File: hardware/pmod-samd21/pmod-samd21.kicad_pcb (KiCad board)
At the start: 2 copper layers, 18 x 29 mm, 19 parts, among them J1 PMOD-2x6-MALE, J2 PMOD-2x6-FEMALE, J3 USB_C_Receptacle_USB2.0, Q1 2N7002PW, U1 ATSAMD21G-A, Y1 32.768kHz

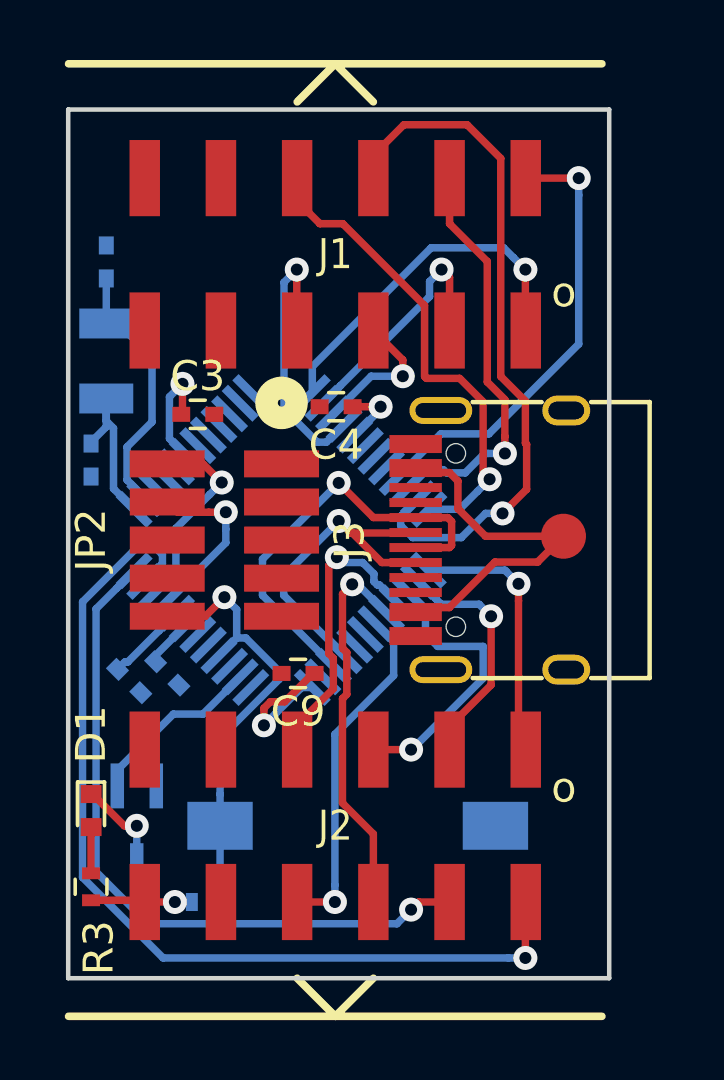
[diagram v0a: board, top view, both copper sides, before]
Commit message: PCB fully routed with DRC errors ignored - oshpark doesn't like the slots in the usb connector - need to check FET pinout
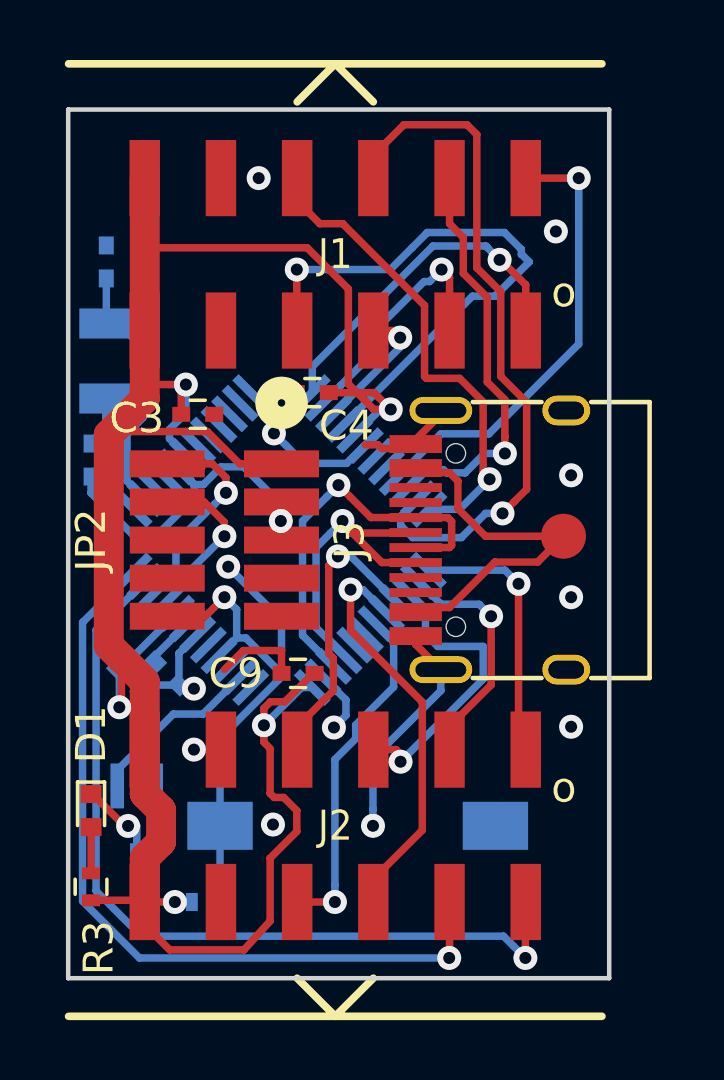
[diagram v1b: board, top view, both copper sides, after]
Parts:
- moved C4 0.92 mm to (150.9, 144.3)
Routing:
- net +3V3: track 17.1 -> 80.4 mm, vias 4 -> 5
- net GND: track 0.30 -> 39.0 mm, vias 0 -> 13
- net /SER0_3: track 9.57 -> 19.2 mm
- net /SER5_0: track 31.7 -> 28.1 mm
- net /SER5_1: track 23.4 -> 26.6 mm
- net /USB_D+: track 14.5 -> 13.3 mm
- net /USB_D-: track 11.9 -> 11.0 mm
- net /SER5_2: track 12.8 -> 13.6 mm
- net /SER1_2: track 9.45 -> 9.95 mm
- added copper zone on B.Cu, net GND
- added copper zone on F.Cu, net GND

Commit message: pcb as submitted to oshpark
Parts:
- TP1: moved to B.Cu
- moved J3 0.40 mm to (157.9, 149.2)
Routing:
- net /SER0_3: track 19.2 -> 9.57 mm
- net GND: track 39.0 -> 46.7 mm, vias 13 -> 12
- net /SER2_2: track 23.5 -> 27.6 mm
- net /SER1_2: track 9.95 -> 6.22 mm
- net /SER2_0: track 15.2 -> 12.8 mm
- net VBUS: track 12.9 -> 11.2 mm, vias 0 -> 1
- net /SER1_1: track 7.92 -> 9.58 mm
- net /SER5_2: track 13.6 -> 12.1 mm
- net /SER2_3: track 16.2 -> 17.6 mm
- net /SER2_1: track 13.7 -> 15.0 mm
- net /USB_D-: track 11.0 -> 11.9 mm
- net /SER5_3: track 11.6 -> 12.2 mm
- net /SER1_3: track 9.74 -> 9.17 mm
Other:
- board size 18 x 29 mm -> 18.2 x 29 mm
- board text added: "Nov 2018"
- board text added: "pmod-samd21"
- board text added: "tom@tomk.in"

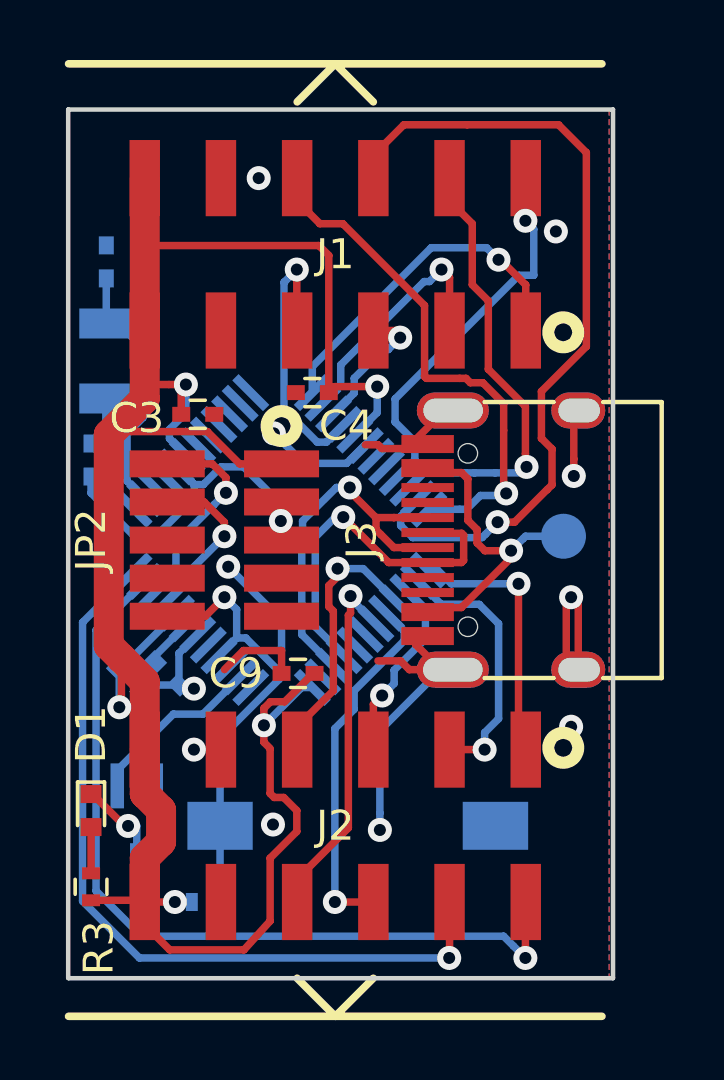
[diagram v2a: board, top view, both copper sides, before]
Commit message: pmod-samd21 : Fixed edge cuts for panelisation with plated slots
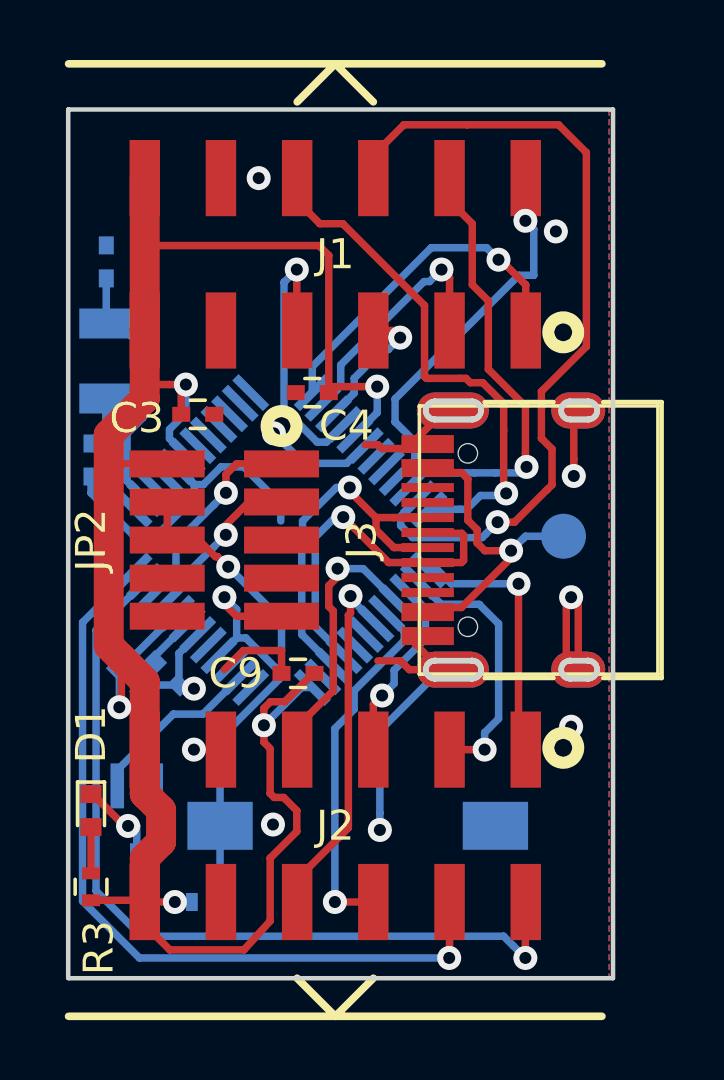
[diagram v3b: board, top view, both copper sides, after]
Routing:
- net GND: track 46.7 -> 50.4 mm, vias 12 -> 11
- net +3V3: track 80.8 -> 77.5 mm
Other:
- board text added: "Dec 2018"
- board text removed: "Nov 2018"

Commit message: pmod-samd21 - added missing usb C resistors - generated gerbers relative to aux origin
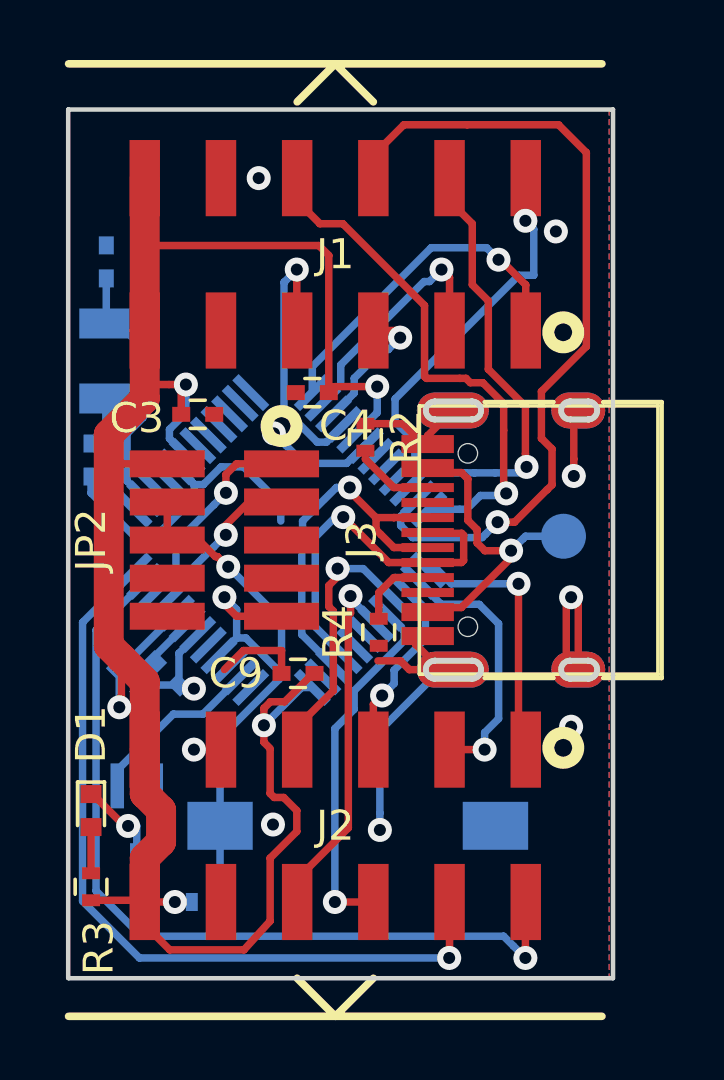
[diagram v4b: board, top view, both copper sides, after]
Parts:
- added R2: 5.1k, Resistors_SMD:R_0402, F.Cu at (152.7, 145.8)
- added R4: 5.1k, Resistors_SMD:R_0402, F.Cu at (153.1, 152.3)
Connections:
- J3 pad A5: (no net) -> Net-(J3-PadA5)
- J3 pad B5: (no net) -> Net-(J3-PadB5)
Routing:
- net Net-(J3-PadA5): track 0.00 -> 2.71 mm
- net Net-(J3-PadB5): track 0.00 -> 2.49 mm
- net GND: track 50.4 -> 51.2 mm
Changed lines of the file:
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@@
     (thickness 1.6)
     (drawings 8)
-    (tracks 413)
+    (tracks 420)
     (zones 0)
-    (modules 19)
-    (nets 31)
+    (modules 21)
+    (nets 33)
   )
   (page A4)
@@
     (pad_to_mask_clearance 0.051)
     (solder_mask_min_width 0.25)
-    (aux_axis_origin 0 0)
+    (aux_axis_origin 142.748 163.8173)
     (visible_elements FFFFFF7F)
     (pcbplotparams
@@
       (viasonmask false)
       (mode 1)
-      (useauxorigin false)
+      (useauxorigin true)
       (hpglpennumber 1)
       (hpglpenspeed 20)
@@
   (net 29 "Net-(D1-Pad1)")
   (net 30 "Net-(D1-Pad2)")
+  (net 31 "Net-(J3-PadB5)")
+  (net 32 "Net-(J3-PadA5)")
   (net_class Default "This is the default net class."
     (clearance 0.2)
@@
     (add_net "Net-(D1-Pad1)")
     (add_net "Net-(D1-Pad2)")
+    (add_net "Net-(J3-PadA5)")
+    (add_net "Net-(J3-PadB5)")
     (add_net VBUS)
   )
@@
       (net 26 /USB_D+))
     (pad A8 smd rect (at 1.25 -3.15 90) (size 0.3 1.75) (layers F.Cu F.Paste F.Mask))
-    (pad B5 smd rect (at 1.75 -3.15 90) (size 0.3 1.75) (layers F.Cu F.Paste F.Mask))
+    (pad B5 smd rect (at 1.75 -3.15 90) (size 0.3 1.75) (layers F.Cu F.Paste F.Mask)
+      (net 31 "Net-(J3-PadB5)"))
     (pad B7 smd rect (at -0.75 -3.15 90) (size 0.3 1.75) (layers F.Cu F.Paste F.Mask)
       (net 27 /USB_D-))
     (pad B8 smd rect (at -1.75 -3.15 90) (size 0.3 1.75) (layers F.Cu F.Paste F.Mask))
-    (pad A5 smd rect (at -1.25 -3.15 90) (size 0.3 1.75) (layers F.Cu F.Paste F.Mask))
+    (pad A5 smd rect (at -1.25 -3.15 90) (size 0.3 1.75) (layers F.Cu F.Paste F.Mask)
+      (net 32 "Net-(J3-PadA5)"))
     (pad A6 smd rect (at -0.25 -3.15 90) (size 0.3 1.75) (layers F.Cu F.Paste F.Mask)
       (net 26 /USB_D+))
@@
       (net 28 VBUS))
   )
+  (module Resistors_SMD:R_0402 (layer F.Cu)
+    (at 152.654 145.796 270)
+    (descr "Resistor SMD 0402, reflow soldering, Vishay (see dcrcw.pdf)")
+    (tags "resistor 0402")
+    (attr smd)
+    (fp_text reference R2 (at 0 -1.35 270) (layer F.SilkS)
+      (effects (font (size 1 1) (thickness 0.15)))
+    )
+    (fp_text value 5.1k (at 0 1.45 270) (layer F.Fab) hide
+      (effects (font (size 1 1) (thickness 0.15)))
+    )
+    (fp_text user %R (at 0 -1.35 270) (layer F.Fab)
+      (effects (font (size 1 1) (thickness 0.15)))
+    )
+    (fp_line (start -0.5 0.25) (end -0.5 -0.25) (layer F.Fab) (width 0.1))
+    (fp_line (start 0.5 0.25) (end -0.5 0.25) (layer F.Fab) (width 0.1))
+    (fp_line (start 0.5 -0.25) (end 0.5 0.25) (layer F.Fab) (width 0.1))
+    (fp_line (start -0.5 -0.25) (end 0.5 -0.25) (layer F.Fab) (width 0.1))
+    (fp_line (start 0.25 -0.53) (end -0.25 -0.53) (layer F.SilkS) (width 0.12))
+    (fp_line (start -0.25 0.53) (end 0.25 0.53) (layer F.SilkS) (width 0.12))
+    (fp_line (start -0.8 -0.45) (end 0.8 -0.45) (layer F.CrtYd) (width 0.05))
+    (fp_line (start -0.8 -0.45) (end -0.8 0.45) (layer F.CrtYd) (width 0.05))
+    (fp_line (start 0.8 0.45) (end 0.8 -0.45) (layer F.CrtYd) (width 0.05))
+    (fp_line (start 0.8 0.45) (end -0.8 0.45) (layer F.CrtYd) (width 0.05))
+    (pad 1 smd rect (at -0.45 0 270) (size 0.4 0.6) (layers F.Cu F.Paste F.Mask)
+      (net 1 GND))
+    (pad 2 smd rect (at 0.45 0 270) (size 0.4 0.6) (layers F.Cu F.Paste F.Mask)
+      (net 31 "Net-(J3-PadB5)"))
+    (model ${KISYS3DMOD}/Resistors_SMD.3dshapes/R_0402.wrl
+      (at (xyz 0 0 0))
+      (scale (xyz 1 1 1))
+      (rotate (xyz 0 0 0))
+    )
+  )
+  (module Resistors_SMD:R_0402 (layer F.Cu)
+    (at 153.1 152.3 90)
+    (descr "Resistor SMD 0402, reflow soldering, Vishay (see dcrcw.pdf)")
+    (tags "resistor 0402")
+    (attr smd)
+    (fp_text reference R4 (at 0 -1.35 90) (layer F.SilkS)
+      (effects (font (size 1 1) (thickness 0.15)))
+    )
+    (fp_text value 5.1k (at 0 1.45 90) (layer F.Fab)
+      (effects (font (size 1 1) (thickness 0.15)))
+    )
+    (fp_line (start 0.8 0.45) (end -0.8 0.45) (layer F.CrtYd) (width 0.05))
+    (fp_line (start 0.8 0.45) (end 0.8 -0.45) (layer F.CrtYd) (width 0.05))
+    (fp_line (start -0.8 -0.45) (end -0.8 0.45) (layer F.CrtYd) (width 0.05))
+    (fp_line (start -0.8 -0.45) (end 0.8 -0.45) (layer F.CrtYd) (width 0.05))
+    (fp_line (start -0.25 0.53) (end 0.25 0.53) (layer F.SilkS) (width 0.12))
+    (fp_line (start 0.25 -0.53) (end -0.25 -0.53) (layer F.SilkS) (width 0.12))
+    (fp_line (start -0.5 -0.25) (end 0.5 -0.25) (layer F.Fab) (width 0.1))
+    (fp_line (start 0.5 -0.25) (end 0.5 0.25) (layer F.Fab) (width 0.1))
+    (fp_line (start 0.5 0.25) (end -0.5 0.25) (layer F.Fab) (width 0.1))
+    (fp_line (start -0.5 0.25) (end -0.5 -0.25) (layer F.Fab) (width 0.1))
+    (fp_text user %R (at 0 -1.35 90) (layer F.Fab)
+      (effects (font (size 1 1) (thickness 0.15)))
+    )
+    (pad 2 smd rect (at 0.45 0 90) (size 0.4 0.6) (layers F.Cu F.Paste F.Mask)
+      (net 32 "Net-(J3-PadA5)"))
+    (pad 1 smd rect (at -0.45 0 90) (size 0.4 0.6) (layers F.Cu F.Paste F.Mask)
+      (net 1 GND))
+    (model ${KISYS3DMOD}/Resistors_SMD.3dshapes/R_0402.wrl
+      (at (xyz 0 0 0))
+      (scale (xyz 1 1 1))
+      (rotate (xyz 0 0 0))
+    )
+  )
   (gr_text "Dec 2018" (at 154.2669 141.1732) (layer B.SilkS)
     (effects (font (size 1.5 1.5) (thickness 0.3)) (justify mirror))
@@
   (via (at 159.004 138.938) (size 0.8) (drill 0.4) (layers F.Cu B.Cu) (net 1))
   (via (at 159.512 151.13) (size 0.8) (drill 0.4) (layers F.Cu B.Cu) (net 1))
-  (segment (start 155.17 145.035) (end 154.33 145.875) (width 0.25) (layer F.Cu) (net 1))
   (segment (start 155.17 144.905) (end 155.17 145.035) (width 0.25) (layer F.Cu) (net 1))
-  (segment (start 153.205 146.175) (end 153.08 146.05) (width 0.25) (layer F.Cu) (net 1))
-  (segment (start 154.33 146.175) (end 153.205 146.175) (width 0.25) (layer F.Cu) (net 1))
-  (segment (start 153.08 146.05) (end 152.654 146.05) (width 0.25) (layer F.Cu) (net 1))
   (via (at 159.512 155.448) (size 0.8) (drill 0.4) (layers F.Cu B.Cu) (net 1))
   (segment (start 149.86 152.908) (end 149.86 153.67) (width 0.25) (layer F.Cu) (net 1))
@@
   (segment (start 148.596284 146.785482) (end 149.835117 148.024315) (width 0.25) (layer B.Cu) (net 1))
   (segment (start 149.835117 148.024315) (end 149.835117 148.59) (width 0.25) (layer B.Cu) (net 1))
-  (segment (start 154.33 145.875) (end 154.33 146.175) (width 0.25) (layer F.Cu) (net 1) (status 30))
   (segment (start 152.027558 146.668549) (end 150.605549 146.668549) (width 0.25) (layer B.Cu) (net 1))
   (segment (start 152.617732 146.078375) (end 152.027558 146.668549) (width 0.25) (layer B.Cu) (net 1))
@@
   (segment (start 147.726341 149.776341) (end 148.075 150.125) (width 0.25) (layer F.Cu) (net 1))
   (segment (start 146.05 147.955) (end 146.05 149.225) (width 0.25) (layer F.Cu) (net 1))
+  (segment (start 154.73 145.745) (end 155.57 144.905) (width 0.25) (layer F.Cu) (net 1))
+  (segment (start 154.73 145.875) (end 154.73 145.745) (width 0.25) (layer F.Cu) (net 1))
+  (segment (start 154.73 146.175) (end 154.73 145.875) (width 0.25) (layer F.Cu) (net 1))
+  (segment (start 153.901 145.346) (end 152.654 145.346) (width 0.25) (layer F.Cu) (net 1))
+  (segment (start 154.73 146.175) (end 153.901 145.346) (width 0.25) (layer F.Cu) (net 1))
   (segment (start 144.736735 153.287604) (end 146.359821 151.664518) (width 0.25) (layer B.Cu) (net 2) (status 20))
   (segment (start 144.638578 153.287604) (end 144.736735 153.287604) (width 0.25) (layer B.Cu) (net 2))
@@
   (via (at 144.743657 158.754706) (size 0.8) (drill 0.4) (layers F.Cu B.Cu) (net 29))
   (segment (start 143.51 160.332) (end 143.51 158.792) (width 0.25) (layer F.Cu) (net 30) (status 30))
+  (segment (start 152.654 146.524) (end 152.654 146.50001) (width 0.25) (layer F.Cu) (net 31))
+  (segment (start 153.605 147.475) (end 152.654 146.524) (width 0.25) (layer F.Cu) (net 31))
+  (segment (start 154.73 147.475) (end 153.605 147.475) (width 0.25) (layer F.Cu) (net 31))
+  (segment (start 153.1 151.4) (end 153.1 151.85) (width 0.25) (layer F.Cu) (net 32))
+  (segment (start 153.1 150.98) (end 153.1 151.4) (width 0.25) (layer F.Cu) (net 32))
+  (segment (start 153.605 150.475) (end 153.1 150.98) (width 0.25) (layer F.Cu) (net 32))
+  (segment (start 154.73 150.475) (end 153.605 150.475) (width 0.25) (layer F.Cu) (net 32))
   (zone (net 1) (net_name GND) (layer F.Cu) (hatch none 0.508)
     (connect_pads (clearance 0.2))
